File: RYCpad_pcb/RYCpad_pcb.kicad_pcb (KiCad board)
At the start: 2 copper layers, 77.2 x 117.6 mm, 65 parts, among them J1 USB_C_Receptacle_USB2.0, J2 AVR ISP, K1 KEYSW, K10 KEYSW, K11 KEYSW, K12 KEYSW, K13 KEYSW, K14 KEYSW, K15 KEYSW, K16 KEYSW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

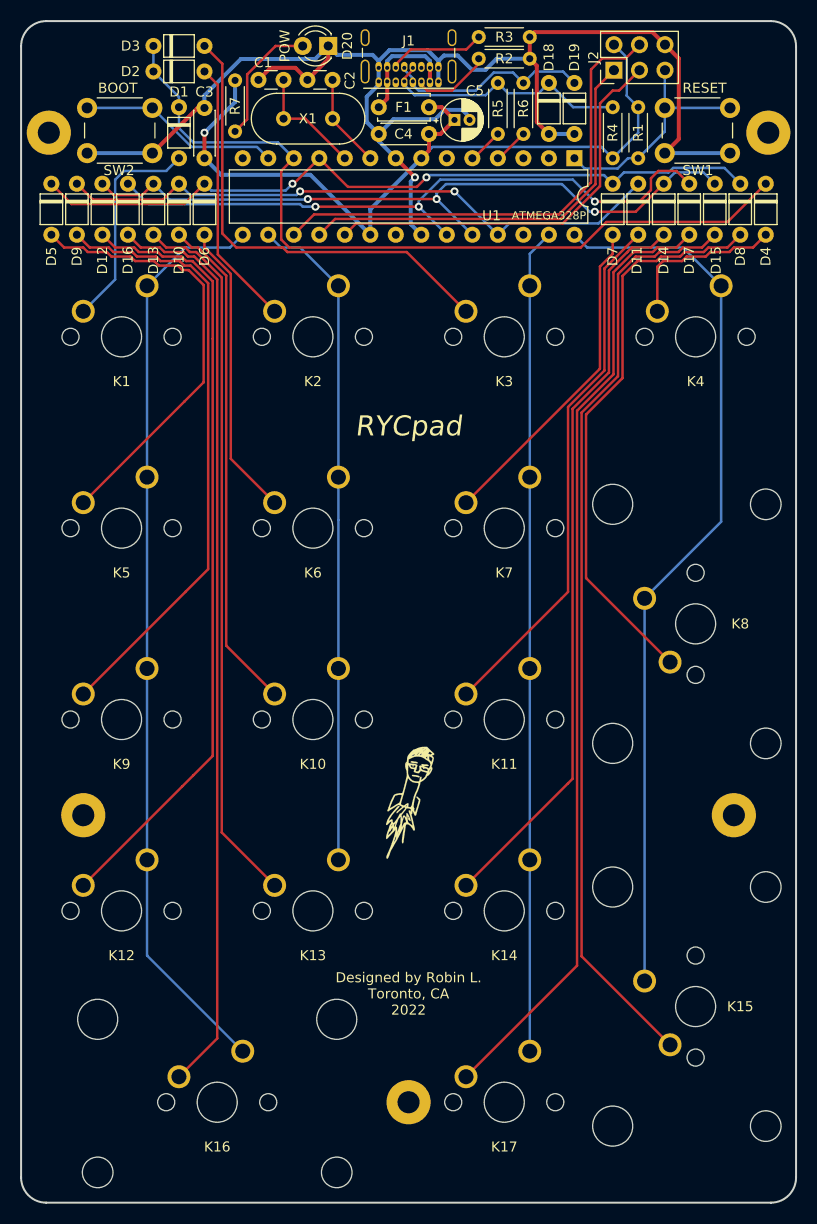
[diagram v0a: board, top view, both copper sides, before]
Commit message: Add logo art
- also, numerous small routing changes
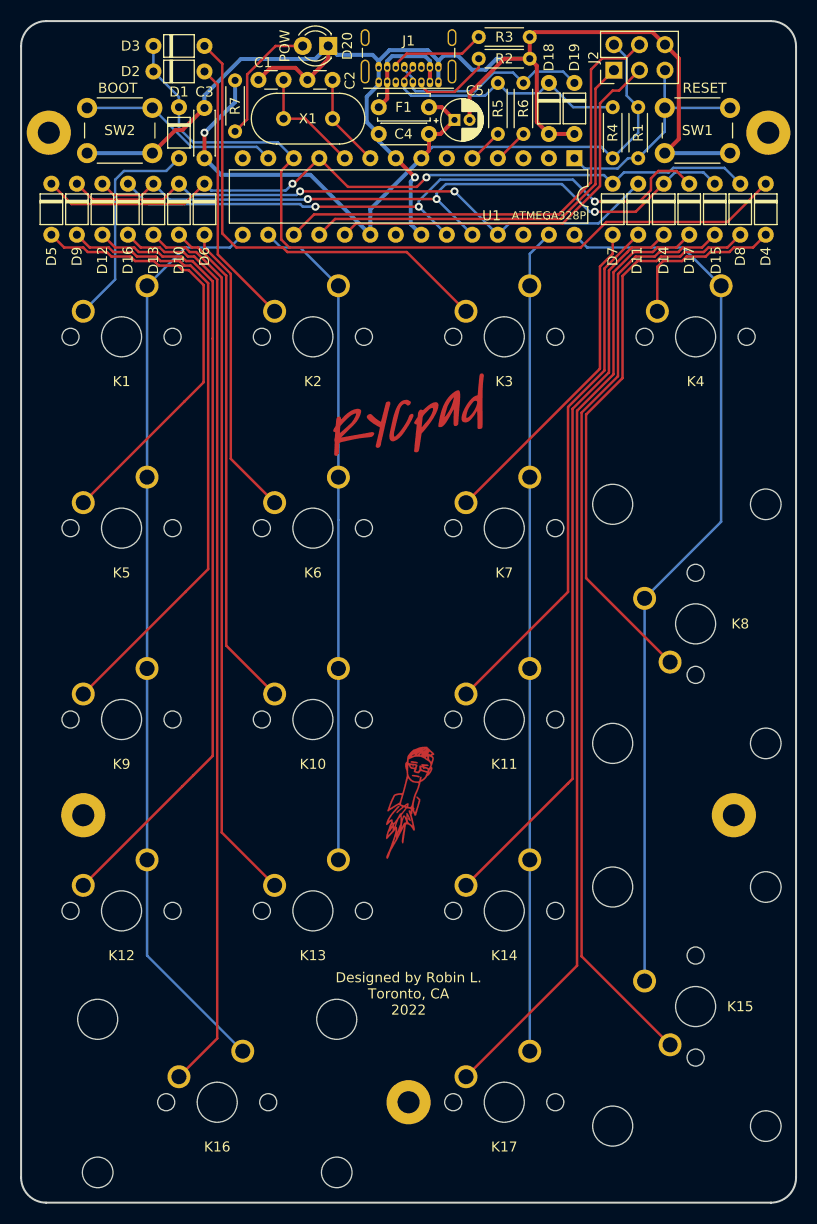
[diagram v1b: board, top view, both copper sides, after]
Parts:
- added G***: LOGO, personal:RYCpad_logo_v0, F.Cu at (0.00, -20.8)
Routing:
- net GND: track 140.8 -> 140.2 mm
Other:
- board text removed: "RYCpad"

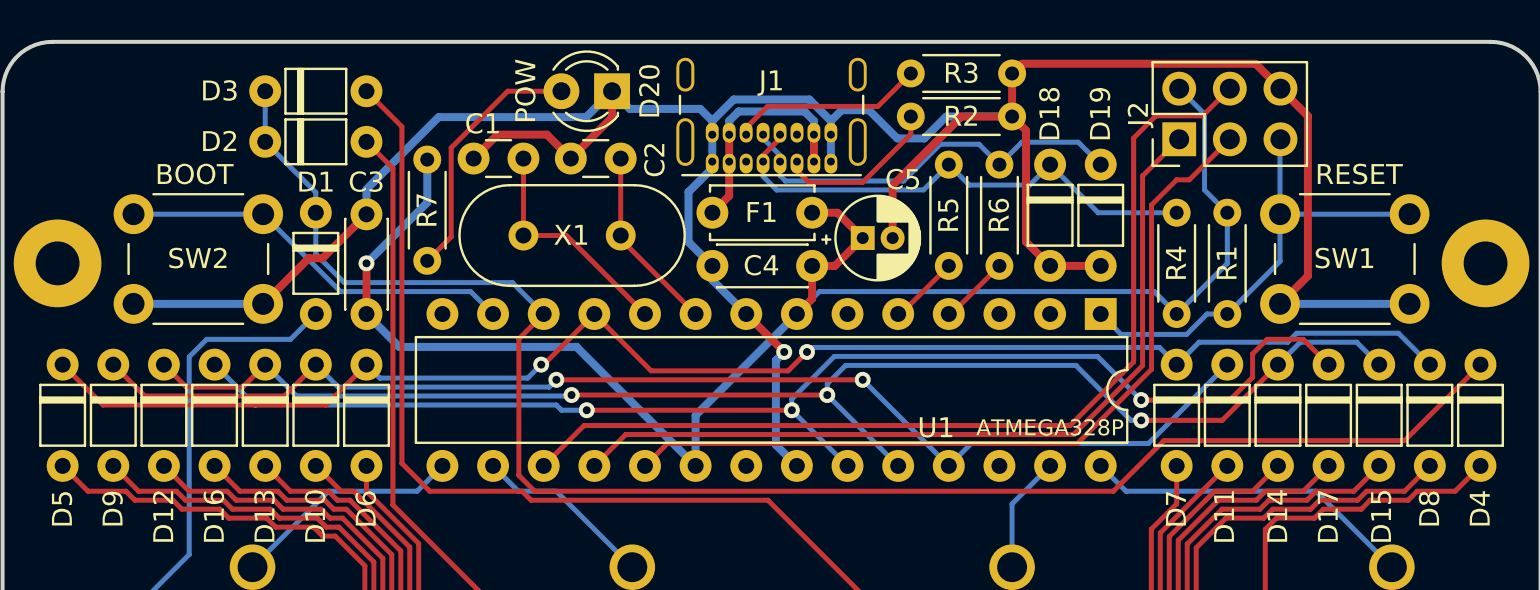
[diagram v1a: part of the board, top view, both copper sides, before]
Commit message: minor routing changes
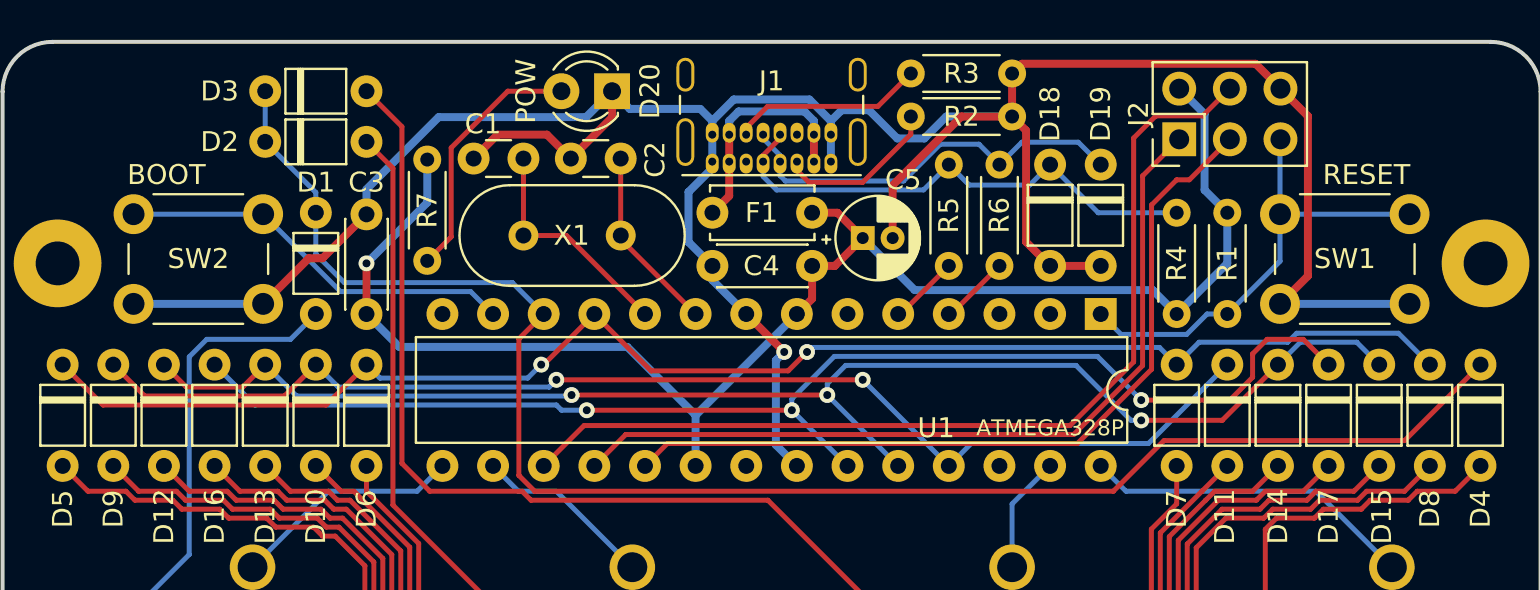
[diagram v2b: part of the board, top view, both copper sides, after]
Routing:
- net +5V: track 80.6 -> 76.9 mm
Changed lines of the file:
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@@
     (effects (font (size 1.5 1.5) (thickness 0.3)) (justify mirror))
   )
-  (gr_text "RESET" (at 29.464 -53.34) (layer "F.SilkS")
+  (gr_text "RESET" (at 29.845 -53.34) (layer "F.SilkS")
     (effects (font (size 1 1) (thickness 0.15)))
   )
@@
     (effects (font (size 1 1) (thickness 0.15)))
   )
-  (gr_text "BOOT" (at -28.956 -53.34) (layer "F.SilkS")
+  (gr_text "BOOT" (at -30.353 -53.34) (layer "F.SilkS")
     (effects (font (size 1 1) (thickness 0.15)))
   )
@@
   (via (at -20.32 -48.895) (size 0.8) (drill 0.4) (layers "F.Cu" "B.Cu") (net 29))
   (segment (start -17.272 -51.943) (end -20.32 -48.895) (width 0.4) (layer "B.Cu") (net 29))
-  (segment (start 22.86 -51.435) (end 21.717 -52.578) (width 0.25) (layer "B.Cu") (net 29))
-  (segment (start 21.717 -56.388) (end 20.447 -57.658) (width 0.25) (layer "B.Cu") (net 29))
+  (segment (start -7.239 -44.704) (end -18.669 -44.704) (width 0.4) (layer "B.Cu") (net 29))
+  (segment (start 4.572 -50.165) (end 7.182489 -47.554511) (width 0.4) (layer "B.Cu") (net 29))
+  (segment (start 7.182489 -47.554511) (end 19.120489 -47.554511) (width 0.4) (layer "B.Cu") (net 29))
   (segment (start -17.272 -54.102) (end -17.272 -51.943) (width 0.4) (layer "B.Cu") (net 29))
-  (segment (start 19.194999 -47.480001) (end 20.32 -46.355) (width 0.25) (layer "B.Cu") (net 29))
-  (segment (start 22.86 -51.435) (end 22.86 -48.895) (width 0.25) (layer "B.Cu") (net 29))
+  (segment (start -3.81 -41.275) (end -7.239 -44.704) (width 0.4) (layer "B.Cu") (net 29))
+  (segment (start 22.86 -51.435) (end 22.86 -48.895) (width 0.4) (layer "B.Cu") (net 29))
   (segment (start -3.81 -41.275) (end 1.27 -46.355) (width 0.4) (layer "B.Cu") (net 29))
-  (segment (start -18.669 -44.704) (end -9.779 -44.704) (width 0.4) (layer "B.Cu") (net 29))
-  (segment (start 22.86 -48.895) (end 20.32 -46.355) (width 0.25) (layer "B.Cu") (net 29))
-  (segment (start 21.717 -52.578) (end 21.717 -56.388) (width 0.25) (layer "B.Cu") (net 29))
-  (segment (start 2.395001 -47.480001) (end 19.194999 -47.480001) (width 0.25) (layer "B.Cu") (net 29))
-  (segment (start 1.27 -46.355) (end 2.395001 -47.480001) (width 0.25) (layer "B.Cu") (net 29))
-  (segment (start -9.779 -44.704) (end -3.81 -38.735) (width 0.4) (layer "B.Cu") (net 29))
-  (segment (start -20.32 -46.355) (end -18.669 -44.704) (width 0.4) (layer "B.Cu") (net 29))
+  (segment (start 22.86 -48.895) (end 20.32 -46.355) (width 0.4) (layer "B.Cu") (net 29))
+  (segment (start 21.72 -56.385) (end 20.447 -57.658) (width 0.4) (layer "B.Cu") (net 29))
+  (segment (start 19.120489 -47.554511) (end 20.32 -46.355) (width 0.4) (layer "B.Cu") (net 29))
+  (segment (start 21.72 -52.575) (end 21.72 -56.385) (width 0.4) (layer "B.Cu") (net 29))
+  (segment (start 22.86 -51.435) (end 21.72 -52.575) (width 0.4) (layer "B.Cu") (net 29))
   (segment (start -3.81 -38.735) (end -3.81 -41.275) (width 0.4) (layer "B.Cu") (net 29))
+  (segment (start -18.669 -44.704) (end -20.32 -46.355) (width 0.4) (layer "B.Cu") (net 29))
   (segment (start 15.154679 -40.310011) (end 18.61052 -43.765853) (width 0.25) (layer "F.Cu") (net 30))
   (segment (start -8.89 -38.735) (end -7.314989 -40.310011) (width 0.25) (layer "F.Cu") (net 30))

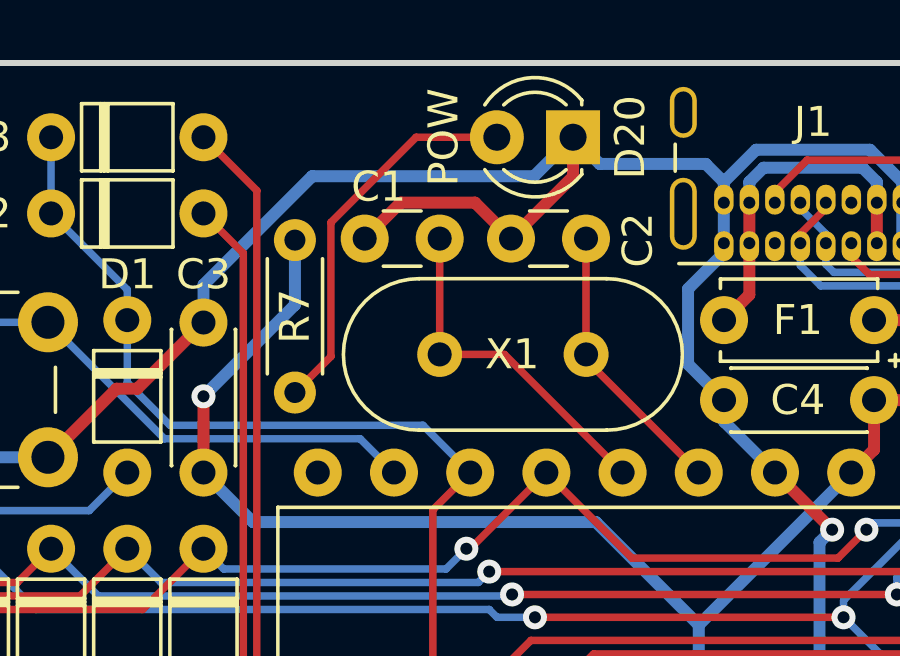
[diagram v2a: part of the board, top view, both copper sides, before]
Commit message: minor routing changes
- also, untrack gerbers
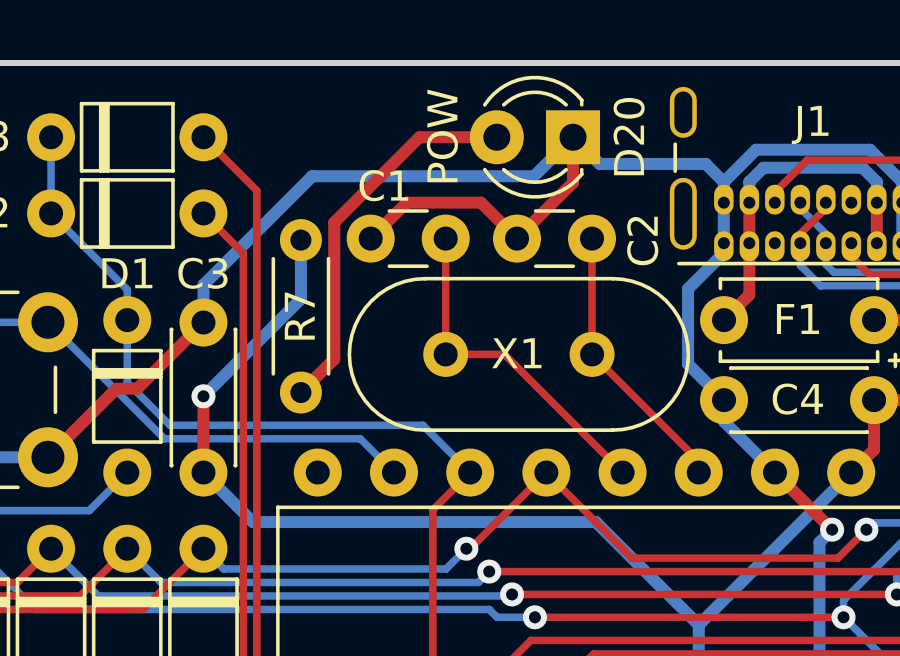
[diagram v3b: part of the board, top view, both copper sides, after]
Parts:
- moved C2 0.20 mm to (-7.37, -54.2)
- moved C1 0.20 mm to (-12.2, -54.2)
- moved R7 0.20 mm to (-17.1, -49.0)
- moved X1 0.20 mm to (-12.2, -50.3)
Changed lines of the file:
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@@
   )
   (footprint "Resistor_THT:R_Axial_DIN0204_L3.6mm_D1.6mm_P5.08mm_Horizontal" (layer "F.Cu")
-    (at -17.272 -49.022 90)
+    (at -17.072 -49.022 90)
     (descr "Resistor, Axial_DIN0204 series, Axial, Horizontal, pin pitch=5.08mm, 0.167W, length*diameter=3.6*1.6mm^2, http://cdn-reichelt.de/documents/datenblatt/B400/1_4W%23YAG.pdf")
     (tags "Resistor Axial_DIN0204 series Axial Horizontal pin pitch 5.08mm 0.167W length 3.6mm diameter 1.6mm")
@@
   )
   (footprint "Crystal:Crystal_HC49-U_Vertical" (layer "F.Cu")
-    (at -12.446 -50.292)
+    (at -12.246 -50.292)
     (descr "Crystal THT HC-49/U http://5hertz.com/pdfs/04404_D.pdf")
     (tags "THT crystalHC-49/U")
@@
   )
   (footprint "Capacitor_THT:C_Disc_D3.0mm_W1.6mm_P2.50mm" (layer "F.Cu")
-    (at -12.446 -54.1528 180)
+    (at -12.246 -54.1528 180)
     (descr "C, Disc series, Radial, pin pitch=2.50mm, , diameter*width=3.0*1.6mm^2, Capacitor, http://www.vishay.com/docs/45233/krseries.pdf")
     (tags "C Disc series Radial pin pitch 2.50mm  diameter 3.0mm width 1.6mm Capacitor")
@@
   )
   (footprint "Capacitor_THT:C_Disc_D3.0mm_W1.6mm_P2.50mm" (layer "F.Cu")
-    (at -7.5692 -54.1528 180)
+    (at -7.3692 -54.1528 180)
     (descr "C, Disc series, Radial, pin pitch=2.50mm, , diameter*width=3.0*1.6mm^2, Capacitor, http://www.vishay.com/docs/45233/krseries.pdf")
     (tags "C Disc series Radial pin pitch 2.50mm  diameter 3.0mm width 1.6mm Capacitor")
@@
   (segment (start 26.903511 -48.262511) (end 26.903511 -56.281489) (width 0.4) (layer "F.Cu") (net 23))
   (segment (start 12.765 -49.973) (end 13.97 -48.768) (width 0.4) (layer "F.Cu") (net 23))
-  (segment (start -11.268711 -55.352311) (end -10.0692 -54.1528) (width 0.4) (layer "F.Cu") (net 23))
+  (segment (start -8.001 -57.531) (end -8.001 -56.021) (width 0.4) (layer "F.Cu") (net 23))
   (segment (start 25.527 -57.658) (end 24.277489 -58.907511) (width 0.4) (layer "F.Cu") (net 23))
   (segment (start -23.218 -49.149) (end -22.526 -49.149) (width 0.4) (layer "F.Cu") (net 23))
+  (segment (start -8.001 -56.021) (end -9.8692 -54.1528) (width 0.4) (layer "F.Cu") (net 23))
   (segment (start 12.765 -55.561) (end 12.765 -49.973) (width 0.4) (layer "F.Cu") (net 23))
   (segment (start 6.072 -52.808) (end 9.525 -56.261) (width 0.4) (layer "F.Cu") (net 23))
-  (segment (start -14.946 -54.1528) (end -13.746489 -55.352311) (width 0.4) (layer "F.Cu") (net 23))
+  (segment (start -11.068711 -55.352311) (end -9.8692 -54.1528) (width 0.4) (layer "F.Cu") (net 23))
+  (segment (start -14.746 -54.1528) (end -13.546489 -55.352311) (width 0.4) (layer "F.Cu") (net 23))
   (segment (start 12.065 -56.261) (end 12.765 -55.561) (width 0.4) (layer "F.Cu") (net 23))
-  (segment (start -10.0692 -54.1528) (end -8.001 -56.221) (width 0.4) (layer "F.Cu") (net 23))
   (segment (start 12.065 -58.42) (end 12.065 -56.261) (width 0.4) (layer "F.Cu") (net 23))
   (segment (start 26.903511 -56.281489) (end 25.527 -57.658) (width 0.4) (layer "F.Cu") (net 23))
+  (segment (start -13.546489 -55.352311) (end -11.068711 -55.352311) (width 0.4) (layer "F.Cu") (net 23))
   (segment (start -22.526 -49.149) (end -20.32 -51.355) (width 0.4) (layer "F.Cu") (net 23))
-  (segment (start -8.001 -56.221) (end -8.001 -57.531) (width 0.4) (layer "F.Cu") (net 23))
-  (segment (start -13.746489 -55.352311) (end -11.268711 -55.352311) (width 0.4) (layer "F.Cu") (net 23))
   (segment (start 24.277489 -58.907511) (end 12.552511 -58.907511) (width 0.4) (layer "F.Cu") (net 23))
   (segment (start 9.525 -56.261) (end 12.065 -56.261) (width 0.4) (layer "F.Cu") (net 23))
@@
   (segment (start 2.032 -51.435) (end 3.302 -51.435) (width 0.4) (layer "F.Cu") (net 29))
   (via (at -20.32 -48.895) (size 0.8) (drill 0.4) (layers "F.Cu" "B.Cu") (net 29))
-  (segment (start -17.272 -51.943) (end -20.32 -48.895) (width 0.4) (layer "B.Cu") (net 29))
   (segment (start -7.239 -44.704) (end -18.669 -44.704) (width 0.4) (layer "B.Cu") (net 29))
   (segment (start 4.572 -50.165) (end 7.182489 -47.554511) (width 0.4) (layer "B.Cu") (net 29))
   (segment (start 7.182489 -47.554511) (end 19.120489 -47.554511) (width 0.4) (layer "B.Cu") (net 29))
-  (segment (start -17.272 -54.102) (end -17.272 -51.943) (width 0.4) (layer "B.Cu") (net 29))
+  (segment (start -17.072 -52.143) (end -17.072 -54.102) (width 0.4) (layer "B.Cu") (net 29))
   (segment (start -3.81 -41.275) (end -7.239 -44.704) (width 0.4) (layer "B.Cu") (net 29))
   (segment (start 22.86 -51.435) (end 22.86 -48.895) (width 0.4) (layer "B.Cu") (net 29))
@@
   (segment (start -3.81 -38.735) (end -3.81 -41.275) (width 0.4) (layer "B.Cu") (net 29))
   (segment (start -18.669 -44.704) (end -20.32 -46.355) (width 0.4) (layer "B.Cu") (net 29))
+  (segment (start -20.32 -48.895) (end -17.072 -52.143) (width 0.4) (layer "B.Cu") (net 29))
   (segment (start 15.154679 -40.310011) (end 18.61052 -43.765853) (width 0.25) (layer "F.Cu") (net 30))
   (segment (start -8.89 -38.735) (end -7.314989 -40.310011) (width 0.25) (layer "F.Cu") (net 30))
@@
   (segment (start 9.017 -46.355) (end 8.89 -46.355) (width 0.25) (layer "F.Cu") (net 38))
   (segment (start 11.43 -48.768) (end 9.017 -46.355) (width 0.25) (layer "F.Cu") (net 38))
-  (segment (start -10.287 -50.292) (end -12.446 -50.292) (width 0.25) (layer "F.Cu") (net 40))
-  (segment (start -6.35 -46.355) (end -10.287 -50.292) (width 0.25) (layer "F.Cu") (net 40))
-  (segment (start -12.446 -54.1528) (end -12.446 -50.292) (width 0.25) (layer "F.Cu") (net 40))
-  (segment (start -3.81 -46.355) (end -7.566 -50.111) (width 0.25) (layer "F.Cu") (net 41))
-  (segment (start -7.5692 -50.2952) (end -7.566 -50.292) (width 0.25) (layer "F.Cu") (net 41))
-  (segment (start -7.5692 -54.1528) (end -7.5692 -50.2952) (width 0.25) (layer "F.Cu") (net 41))
-  (segment (start -7.566 -50.111) (end -7.566 -50.292) (width 0.25) (layer "F.Cu") (net 41))
+  (segment (start -12.246 -54.1528) (end -12.246 -50.292) (width 0.25) (layer "F.Cu") (net 40))
+  (segment (start -10.287 -50.292) (end -6.35 -46.355) (width 0.25) (layer "F.Cu") (net 40))
+  (segment (start -12.246 -50.292) (end -10.287 -50.292) (width 0.25) (layer "F.Cu") (net 40))
+  (segment (start -7.366 -50.292) (end -3.81 -46.736) (width 0.25) (layer "F.Cu") (net 41))
+  (segment (start -3.81 -46.736) (end -3.81 -46.355) (width 0.25) (layer "F.Cu") (net 41))
+  (segment (start -7.3692 -50.2952) (end -7.366 -50.292) (width 0.25) (layer "F.Cu") (net 41))
+  (segment (start -7.3692 -54.1528) (end -7.3692 -50.2952) (width 0.25) (layer "F.Cu") (net 41))
   (segment (start -2.125 -54) (end -2.125 -55.35) (width 0.4) (layer "F.Cu") (net 47))
   (segment (start -2.968 -51.435) (end -2.125 -52.278) (width 0.4) (layer "F.Cu") (net 47))
@@
   (segment (start 1.651 -56.515) (end 2.125 -56.041) (width 0.4) (layer "B.Cu") (net 47))
   (segment (start 2.125 -56.041) (end 2.125 -55.35) (width 0.4) (layer "B.Cu") (net 47))
-  (segment (start -16.071001 -54.692801) (end -13.232802 -57.531) (width 0.25) (layer "F.Cu") (net 51))
-  (segment (start -17.272 -49.022) (end -16.071001 -50.222999) (width 0.25) (layer "F.Cu") (net 51))
-  (segment (start -16.071001 -50.222999) (end -16.071001 -54.692801) (width 0.25) (layer "F.Cu") (net 51))
-  (segment (start -13.232802 -57.531) (end -10.541 -57.531) (width 0.25) (layer "F.Cu") (net 51))
+  (segment (start -15.96 -54.69) (end -13.119 -57.531) (width 0.4) (layer "F.Cu") (net 51))
+  (segment (start -17.072 -49.022) (end -15.96 -50.134) (width 0.4) (layer "F.Cu") (net 51))
+  (segment (start -13.119 -57.531) (end -10.541 -57.531) (width 0.4) (layer "F.Cu") (net 51))
+  (segment (start -15.96 -50.134) (end -15.96 -54.69) (width 0.4) (layer "F.Cu") (net 51))
   (segment (start -21.621001 -47.480001) (end -25.504 -51.363) (width 0.25) (layer "B.Cu") (net 52))
   (segment (start -25.504 -51.363) (end -32.004 -51.363) (width 0.25) (layer "B.Cu") (net 52))
